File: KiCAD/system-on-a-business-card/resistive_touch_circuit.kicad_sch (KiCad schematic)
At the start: 50 parts, among them Q10 2N7002K, Q11 2N7002K, Q12 2N7002K, Q3 2N7002K, Q4 2N7002K, Q5 2N7002K, Q6 2N7002K, Q7 2N7002K, Q8 2N7002K, Q9 2N7002K

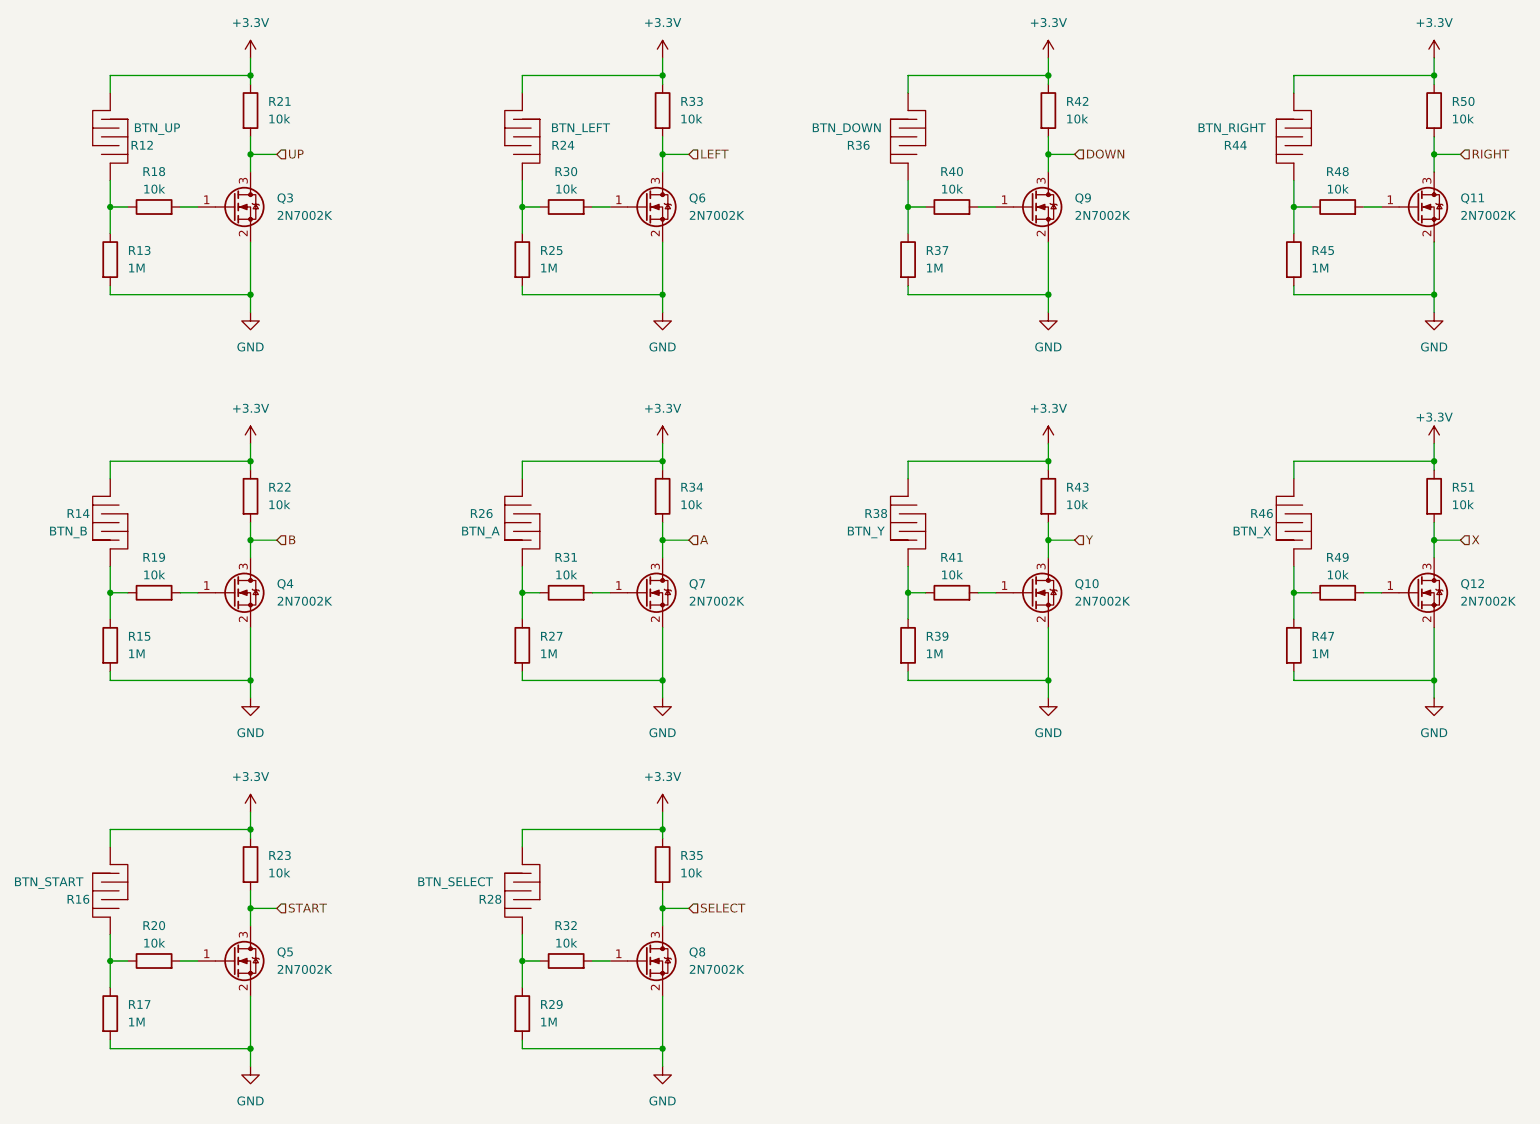
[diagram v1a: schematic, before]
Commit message: #10: added buzzer, io-expander, removed transistors from resistive pad cirucit
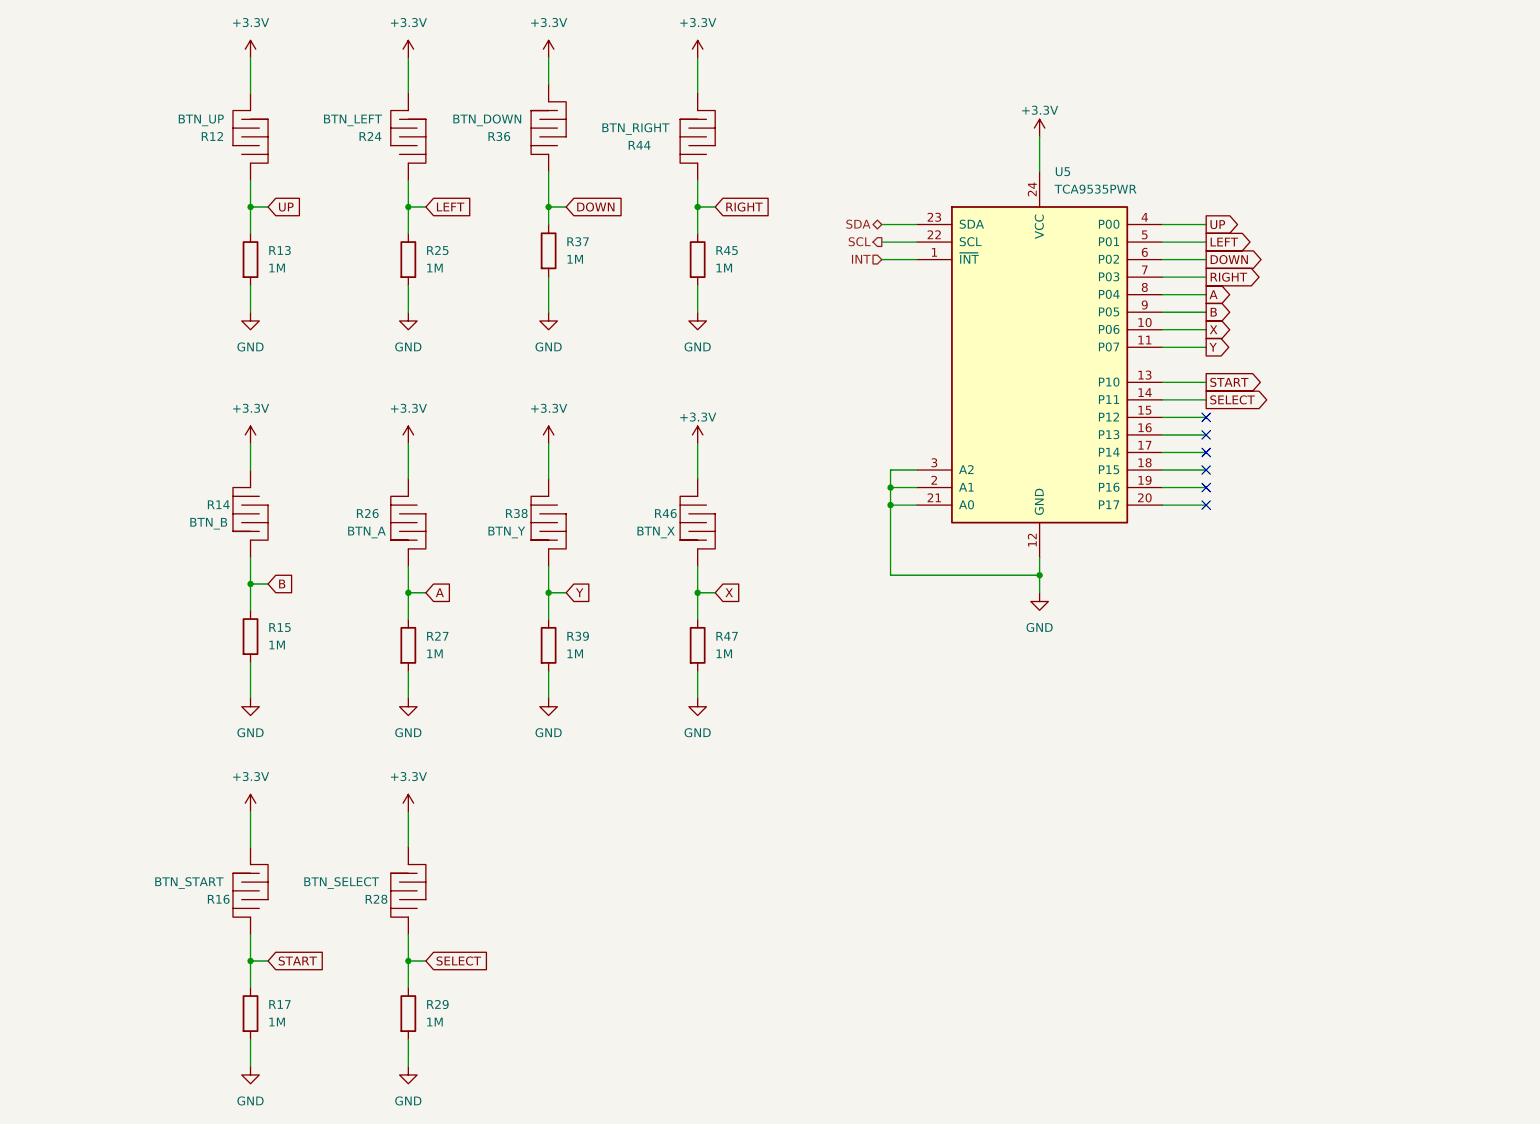
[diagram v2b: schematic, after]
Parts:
- removed Q10, Q11, Q12, Q3, Q4, Q5, Q6, Q7, Q8, Q9: 2N7002K, Package_TO_SOT_SMD:SOT-23, symbol Transistor_FET:2N7002K
- removed R18, R19, R20, R21, R22, R23, R30, R31, R32, R33, R34, R35, R40, R41, R42, R43, R48, R49, R50, R51: 10k, Resistor_SMD:R_0402_1005Metric_Pad0.72x0.64mm_HandSolder, symbol Device:R
- added U5: TCA9535PWR, Package_SO:TSSOP-24_4.4x7.8mm_P0.65mm, symbol Interface_Expansion:TCA9535PWR
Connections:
- net +3.3V: now also U5.24 (VCC)
- net A: now also R26.2, R27.1, U5.8 (P04)
- net B: now also R14.2, R15.1, U5.9 (P05)
- net DOWN: now also R36.1, R37.1, U5.6 (P02)
- net GND: now also U5.12 (GND), U5.2 (A1), U5.21 (A0), U5.3 (A2)
- net LEFT: now also R24.1, R25.1, U5.5 (P01)
- net RIGHT: now also R44.1, R45.1, U5.7 (P03)
- net SELECT: now also R28.1, R29.1, U5.14 (P11)
- net START: now also R16.1, R17.1, U5.13 (P10)
- net UP: now also R12.1, R13.1, U5.4 (P00)
- net X: now also R46.2, R47.1, U5.10 (P06)
- net Y: now also R38.2, R39.1, U5.11 (P07)
- new net INT: U5.1 (~{INT})
- new net SCL: U5.22 (SCL)
- new net SDA: U5.23 (SDA)
- no-connect marks 0 -> 6
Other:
- moved on the sheet: R12, R13, R14, R15, R16, R17, R24, R25, R26, R27, R28, R29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

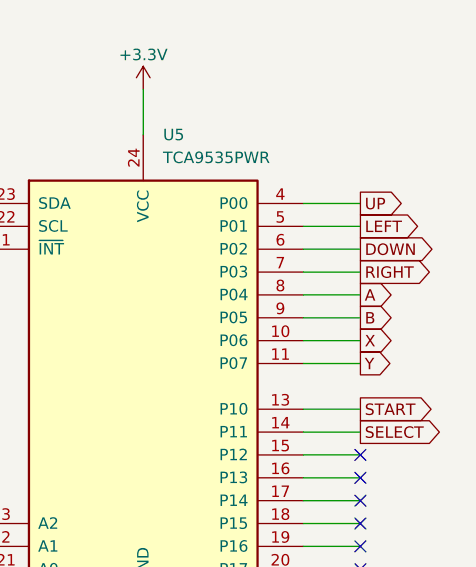
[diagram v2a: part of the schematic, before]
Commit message: #10: continued layouting, added 2nd buzzer
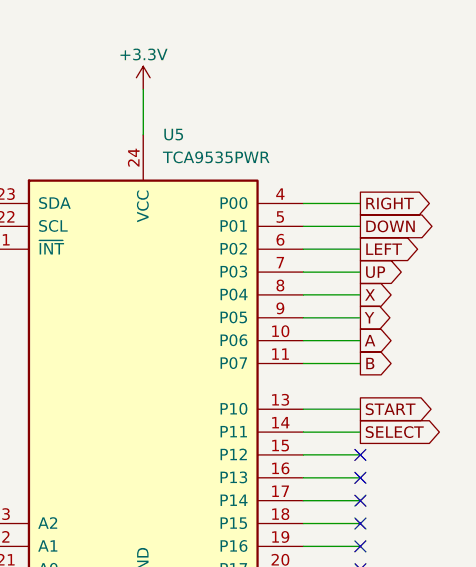
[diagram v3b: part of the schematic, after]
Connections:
- net A: now also U5.10 (P06); no longer U5.8 (P04)
- net B: now also U5.11 (P07); no longer U5.9 (P05)
- net DOWN: now also U5.5 (P01); no longer U5.6 (P02)
- net LEFT: now also U5.6 (P02); no longer U5.5 (P01)
- net RIGHT: now also U5.4 (P00); no longer U5.7 (P03)
- net UP: now also U5.7 (P03); no longer U5.4 (P00)
- net X: now also U5.8 (P04); no longer U5.10 (P06)
- net Y: now also U5.9 (P05); no longer U5.11 (P07)
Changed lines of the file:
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@@
     )
   )
-  (global_label "X" (shape output) (at 195.58 60.96 0) (fields_autoplaced)
+  (global_label "X" (shape output) (at 195.58 55.88 0) (fields_autoplaced)
     (effects (font (size 1.27 1.27)) (justify left))
-    (property "Intersheetrefs" "${INTERSHEET_REFS}" (at 199.7747 60.96 0)
+    (property "Intersheetrefs" "${INTERSHEET_REFS}" (at 199.7747 55.88 0)
       (effects (font (size 1.27 1.27)) (justify left) hide)
     )
@@
     )
   )
-  (global_label "B" (shape output) (at 195.58 58.42 0) (fields_autoplaced)
+  (global_label "B" (shape output) (at 195.58 63.5 0) (fields_autoplaced)
     (effects (font (size 1.27 1.27)) (justify left))
-    (property "Intersheetrefs" "${INTERSHEET_REFS}" (at 199.8352 58.42 0)
+    (property "Intersheetrefs" "${INTERSHEET_REFS}" (at 199.8352 63.5 0)
       (effects (font (size 1.27 1.27)) (justify left) hide)
     )
@@
     )
   )
-  (global_label "UP" (shape output) (at 195.58 45.72 0) (fields_autoplaced)
+  (global_label "UP" (shape output) (at 195.58 53.34 0) (fields_autoplaced)
     (effects (font (size 1.27 1.27)) (justify left))
-    (property "Intersheetrefs" "${INTERSHEET_REFS}" (at 201.1657 45.72 0)
+    (property "Intersheetrefs" "${INTERSHEET_REFS}" (at 201.1657 53.34 0)
       (effects (font (size 1.27 1.27)) (justify left) hide)
     )
@@
     )
   )
-  (global_label "Y" (shape output) (at 195.58 63.5 0) (fields_autoplaced)
+  (global_label "Y" (shape output) (at 195.58 58.42 0) (fields_autoplaced)
     (effects (font (size 1.27 1.27)) (justify left))
-    (property "Intersheetrefs" "${INTERSHEET_REFS}" (at 199.6538 63.5 0)
+    (property "Intersheetrefs" "${INTERSHEET_REFS}" (at 199.6538 58.42 0)
       (effects (font (size 1.27 1.27)) (justify left) hide)
     )
@@
     )
   )
-  (global_label "LEFT" (shape output) (at 195.58 48.26 0) (fields_autoplaced)
+  (global_label "LEFT" (shape output) (at 195.58 50.8 0) (fields_autoplaced)
     (effects (font (size 1.27 1.27)) (justify left))
-    (property "Intersheetrefs" "${INTERSHEET_REFS}" (at 202.7985 48.26 0)
+    (property "Intersheetrefs" "${INTERSHEET_REFS}" (at 202.7985 50.8 0)
       (effects (font (size 1.27 1.27)) (justify left) hide)
     )
   )
-  (global_label "A" (shape output) (at 195.58 55.88 0) (fields_autoplaced)
+  (global_label "A" (shape output) (at 195.58 60.96 0) (fields_autoplaced)
     (effects (font (size 1.27 1.27)) (justify left))
-    (property "Intersheetrefs" "${INTERSHEET_REFS}" (at 199.6538 55.88 0)
+    (property "Intersheetrefs" "${INTERSHEET_REFS}" (at 199.6538 60.96 0)
       (effects (font (size 1.27 1.27)) (justify left) hide)
     )
@@
     )
   )
-  (global_label "DOWN" (shape output) (at 195.58 50.8 0) (fields_autoplaced)
+  (global_label "DOWN" (shape output) (at 195.58 48.26 0) (fields_autoplaced)
     (effects (font (size 1.27 1.27)) (justify left))
-    (property "Intersheetrefs" "${INTERSHEET_REFS}" (at 203.9476 50.8 0)
+    (property "Intersheetrefs" "${INTERSHEET_REFS}" (at 203.9476 48.26 0)
       (effects (font (size 1.27 1.27)) (justify left) hide)
     )
   )
-  (global_label "RIGHT" (shape output) (at 195.58 53.34 0) (fields_autoplaced)
+  (global_label "RIGHT" (shape output) (at 195.58 45.72 0) (fields_autoplaced)
     (effects (font (size 1.27 1.27)) (justify left))
-    (property "Intersheetrefs" "${INTERSHEET_REFS}" (at 204.0081 53.34 0)
+    (property "Intersheetrefs" "${INTERSHEET_REFS}" (at 204.0081 45.72 0)
       (effects (font (size 1.27 1.27)) (justify left) hide)
     )

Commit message: #10: started with routing
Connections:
- net B: now also U5.8 (P04); no longer U5.11 (P07)
- net DOWN: now also U5.7 (P03); no longer U5.5 (P01)
- net RIGHT: now also U5.5 (P01); no longer U5.4 (P00)
- net UP: now also U5.4 (P00); no longer U5.7 (P03)
- net X: now also U5.11 (P07); no longer U5.8 (P04)
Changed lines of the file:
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@@
     )
   )
-  (global_label "X" (shape output) (at 195.58 55.88 0) (fields_autoplaced)
+  (global_label "X" (shape output) (at 195.58 63.5 0) (fields_autoplaced)
     (effects (font (size 1.27 1.27)) (justify left))
-    (property "Intersheetrefs" "${INTERSHEET_REFS}" (at 199.7747 55.88 0)
+    (property "Intersheetrefs" "${INTERSHEET_REFS}" (at 199.7747 63.5 0)
       (effects (font (size 1.27 1.27)) (justify left) hide)
     )
@@
     )
   )
-  (global_label "B" (shape output) (at 195.58 63.5 0) (fields_autoplaced)
+  (global_label "B" (shape output) (at 195.58 55.88 0) (fields_autoplaced)
     (effects (font (size 1.27 1.27)) (justify left))
-    (property "Intersheetrefs" "${INTERSHEET_REFS}" (at 199.8352 63.5 0)
+    (property "Intersheetrefs" "${INTERSHEET_REFS}" (at 199.8352 55.88 0)
       (effects (font (size 1.27 1.27)) (justify left) hide)
     )
@@
     )
   )
-  (global_label "UP" (shape output) (at 195.58 53.34 0) (fields_autoplaced)
+  (global_label "UP" (shape output) (at 195.58 45.72 0) (fields_autoplaced)
     (effects (font (size 1.27 1.27)) (justify left))
-    (property "Intersheetrefs" "${INTERSHEET_REFS}" (at 201.1657 53.34 0)
+    (property "Intersheetrefs" "${INTERSHEET_REFS}" (at 201.1657 45.72 0)
       (effects (font (size 1.27 1.27)) (justify left) hide)
     )
@@
     )
   )
-  (global_label "DOWN" (shape output) (at 195.58 48.26 0) (fields_autoplaced)
+  (global_label "DOWN" (shape output) (at 195.58 53.34 0) (fields_autoplaced)
     (effects (font (size 1.27 1.27)) (justify left))
-    (property "Intersheetrefs" "${INTERSHEET_REFS}" (at 203.9476 48.26 0)
+    (property "Intersheetrefs" "${INTERSHEET_REFS}" (at 203.9476 53.34 0)
       (effects (font (size 1.27 1.27)) (justify left) hide)
     )
   )
-  (global_label "RIGHT" (shape output) (at 195.58 45.72 0) (fields_autoplaced)
+  (global_label "RIGHT" (shape output) (at 195.58 48.26 0) (fields_autoplaced)
     (effects (font (size 1.27 1.27)) (justify left))
-    (property "Intersheetrefs" "${INTERSHEET_REFS}" (at 204.0081 45.72 0)
+    (property "Intersheetrefs" "${INTERSHEET_REFS}" (at 204.0081 48.26 0)
       (effects (font (size 1.27 1.27)) (justify left) hide)
     )

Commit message: #10: continued with routing
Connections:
- net B: now also U5.9 (P05); no longer U5.8 (P04)
- net Y: now also U5.8 (P04); no longer U5.9 (P05)
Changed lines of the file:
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@@
     )
   )
-  (global_label "B" (shape output) (at 195.58 55.88 0) (fields_autoplaced)
+  (global_label "B" (shape output) (at 195.58 58.42 0) (fields_autoplaced)
     (effects (font (size 1.27 1.27)) (justify left))
-    (property "Intersheetrefs" "${INTERSHEET_REFS}" (at 199.8352 55.88 0)
+    (property "Intersheetrefs" "${INTERSHEET_REFS}" (at 199.8352 58.42 0)
       (effects (font (size 1.27 1.27)) (justify left) hide)
     )
@@
     )
   )
-  (global_label "Y" (shape output) (at 195.58 58.42 0) (fields_autoplaced)
+  (global_label "Y" (shape output) (at 195.58 55.88 0) (fields_autoplaced)
     (effects (font (size 1.27 1.27)) (justify left))
-    (property "Intersheetrefs" "${INTERSHEET_REFS}" (at 199.6538 58.42 0)
+    (property "Intersheetrefs" "${INTERSHEET_REFS}" (at 199.6538 55.88 0)
       (effects (font (size 1.27 1.27)) (justify left) hide)
     )

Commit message: #10: finished initial routing
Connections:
- net SDCard_DET: now reaches U5.15 (P12)
- no-connect marks 6 -> 5
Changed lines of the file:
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@@
   (junction (at 171.45 96.52) (diameter 0) (color 0 0 0 0)
   )
-  (no_connect (at 195.58 73.66))
   (no_connect (at 195.58 86.36))
   (no_connect (at 195.58 83.82))
@@
     (effects (font (size 1.27 1.27)) (justify right))
   )
+  (hierarchical_label "SDCard_DET" (shape output) (at 195.58 73.66 0) (fields_autoplaced)
+    (effects (font (size 1.27 1.27)) (justify left))
+  )
   (hierarchical_label "SCL" (shape output) (at 148.59 48.26 180) (fields_autoplaced)

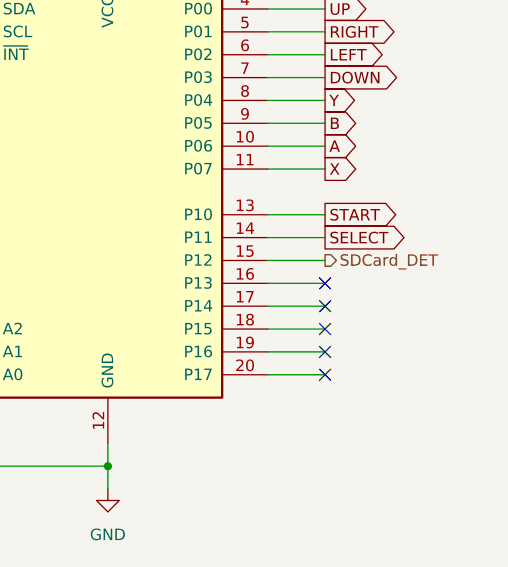
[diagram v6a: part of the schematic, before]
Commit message: #10: connected display reset to GPIO Expander
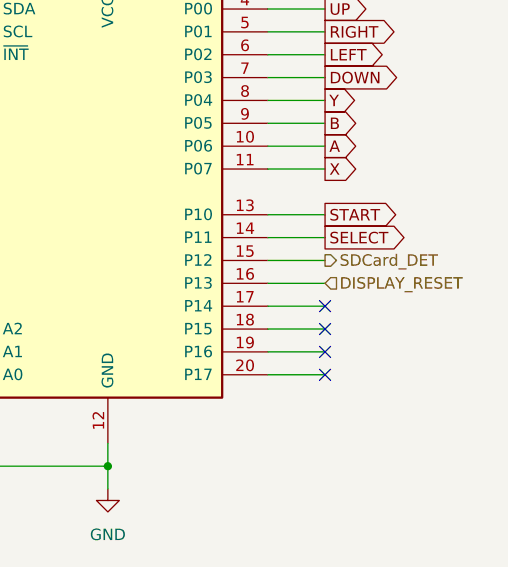
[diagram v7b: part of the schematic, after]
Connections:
- net DISPLAY_RESET: now reaches U5.16 (P13)
- no-connect marks 5 -> 4
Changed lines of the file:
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@@
   (no_connect (at 195.58 78.74))
   (no_connect (at 195.58 81.28))
-  (no_connect (at 195.58 76.2))
   (wire (pts (xy 149.86 83.82) (xy 149.86 86.36))
     (stroke (width 0) (type default))
@@
     )
   )
+  (hierarchical_label "DISPLAY_RESET" (shape input) (at 195.58 76.2 0) (fields_autoplaced)
+    (effects (font (size 1.27 1.27)) (justify left))
+  )
   (hierarchical_label "SDA" (shape bidirectional) (at 148.59 45.72 180) (fields_autoplaced)
